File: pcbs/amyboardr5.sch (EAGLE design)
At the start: 152 parts, among them Q2 S8050, Q5 S8050, U1 PCM9211PT, U15 H11L1SR2M, U16 SPX3819, U2 ESP32­S2­SOLO, U3 SPX3819, U4 TL074CD, U6 HX3608, Y1 22.5792MHZ

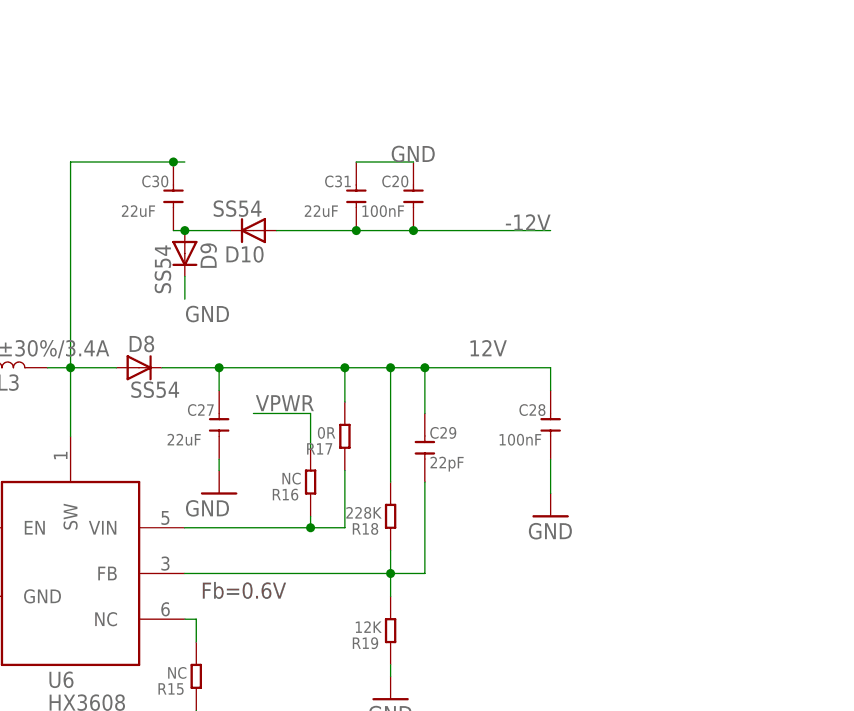
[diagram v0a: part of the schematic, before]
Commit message: Added ferrite beads in Pi circuits to + and -12v lines.
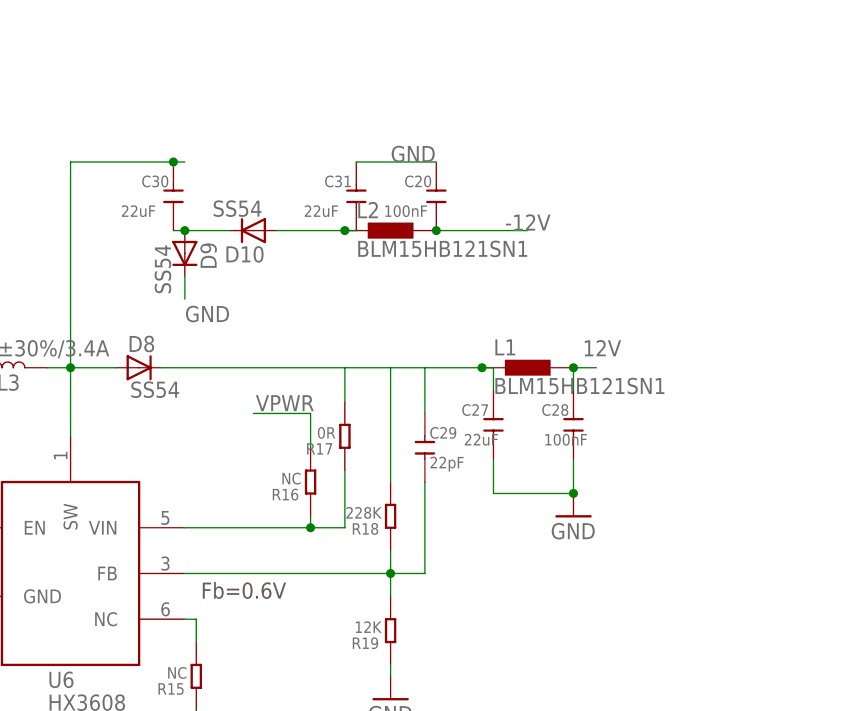
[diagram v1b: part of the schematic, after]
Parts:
- added L1, L2: BLM15HB121SN1, inductors:BLM15HB121SN1
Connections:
- new net N$16: C31.2, D10.A, L2.1
- new net N$24: C27.1, D8.C, L1.1
- new net N$25: C29.1
- new net N$30: R18.2
- net -12V: now also L2.2; no longer C31.2, D10.A
- net 12V: now also L1.2; no longer C27.1, C29.1, D8.C, R18.2
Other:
- moved on the sheet: C20, C27, C28
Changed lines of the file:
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@@
 <part name="GND5" library="supply1" deviceset="GND" device=""/>
 <part name="R14" library="A9G" deviceset="DISCRETE_R*" device="-0603" value="100K"/>
-<part name="GND6" library="supply1" deviceset="GND" device=""/>
 <part name="R15" library="A9G" deviceset="DISCRETE_R*" device="-0603" value="NC"/>
 <part name="R16" library="A9G" deviceset="DISCRETE_R*" device="-0603" value="NC"/>
@@
 <part name="R6" library="adafruit" deviceset="R-US_" device="R0805" value="10K"/>
 <part name="R8" library="adafruit" deviceset="R-US_" device="R0805" value="15K"/>
+<part name="L1" library="inductors" library_urn="urn:adsk.eagle:library:243" deviceset="BLM15H" device="" package3d_urn="urn:adsk.eagle:package:15132/1" technology="B121SN1"/>
+<part name="L2" library="inductors" library_urn="urn:adsk.eagle:library:243" deviceset="BLM15H" device="" package3d_urn="urn:adsk.eagle:package:15132/1" technology="B121SN1"/>
 </parts>
 <sheets>
@@
 <attribute name="VALUE" x="242.824" y="-8.4074" size="1.778" layer="96"/>
 </instance>
-<instance part="C27" gate="C" x="252.73" y="-11.43" smashed="yes" rot="R270">
-<attribute name="NAME" x="249.174" y="-10.414" size="1.27" layer="95" ratio="10"/>
-<attribute name="VALUE" x="246.888" y="-13.716" size="1.27" layer="96" ratio="10"/>
-</instance>
-<instance part="C28" gate="C" x="289.56" y="-11.43" smashed="yes" rot="R270">
-<attribute name="NAME" x="286.004" y="-10.414" size="1.27" layer="95" ratio="10"/>
-<attribute name="VALUE" x="283.718" y="-13.716" size="1.27" layer="96" ratio="10"/>
+<instance part="C27" gate="C" x="283.21" y="-11.43" smashed="yes" rot="R270">
+<attribute name="NAME" x="279.654" y="-10.414" size="1.27" layer="95" ratio="10"/>
+<attribute name="VALUE" x="279.908" y="-13.716" size="1.27" layer="96" ratio="10"/>
+</instance>
+<instance part="C28" gate="C" x="292.1" y="-11.43" smashed="yes" rot="R270">
+<attribute name="NAME" x="288.544" y="-10.414" size="1.27" layer="95" ratio="10"/>
+<attribute name="VALUE" x="288.798" y="-13.716" size="1.27" layer="96" ratio="10"/>
 </instance>
 <instance part="C29" gate="C" x="275.59" y="-13.97" smashed="yes" rot="R270">
@@
 <attribute name="VALUE" x="269.24" y="-44.45" size="1.778" layer="96"/>
 </instance>
-<instance part="GND5" gate="1" x="289.56" y="-21.59" smashed="yes">
-<attribute name="VALUE" x="287.02" y="-24.13" size="1.778" layer="96"/>
+<instance part="GND5" gate="1" x="292.1" y="-21.59" smashed="yes">
+<attribute name="VALUE" x="289.56" y="-24.13" size="1.778" layer="96"/>
 </instance>
 <instance part="R14" gate="R" x="220.98" y="-13.97" smashed="yes" rot="R90">
@@
 <attribute name="VALUE" x="219.964" y="-12.954" size="1.27" layer="96" ratio="10" rot="R180"/>
 </instance>
-<instance part="GND6" gate="1" x="252.73" y="-19.05" smashed="yes">
-<attribute name="VALUE" x="248.92" y="-21.59" size="1.778" layer="96"/>
-</instance>
 <instance part="R15" gate="R" x="250.19" y="-39.37" smashed="yes" rot="R90">
 <attribute name="NAME" x="248.92" y="-40.132" size="1.27" layer="95" ratio="10" rot="R180"/>
@@
 <attribute name="VALUE" x="262.128" y="11.684" size="1.27" layer="96" ratio="10"/>
 </instance>
-<instance part="C20" gate="C" x="274.32" y="13.97" smashed="yes" rot="R270">
-<attribute name="NAME" x="270.764" y="14.986" size="1.27" layer="95" ratio="10"/>
-<attribute name="VALUE" x="268.478" y="11.684" size="1.27" layer="96" ratio="10"/>
+<instance part="C20" gate="C" x="276.86" y="13.97" smashed="yes" rot="R270">
+<attribute name="NAME" x="273.304" y="14.986" size="1.27" layer="95" ratio="10"/>
+<attribute name="VALUE" x="271.018" y="11.684" size="1.27" layer="96" ratio="10"/>
 </instance>
 <instance part="C21" gate="C" x="-137.16" y="-46.99" smashed="yes" rot="R270">
@@
 <attribute name="VALUE" x="-99.06" y="-28.702" size="1.016" layer="96" font="vector" ratio="15" rot="R270"/>
 </instance>
+<instance part="L1" gate="G$1" x="287.02" y="-5.08" smashed="yes">
+<attribute name="NAME" x="283.21" y="-3.7084" size="1.778" layer="95"/>
+<attribute name="VALUE" x="283.21" y="-8.001" size="1.778" layer="96"/>
+</instance>
+<instance part="L2" gate="G$1" x="271.78" y="10.16" smashed="yes">
+<attribute name="NAME" x="267.97" y="11.5316" size="1.778" layer="95"/>
+<attribute name="VALUE" x="267.97" y="7.239" size="1.778" layer="96"/>
+</instance>
 </instances>
 <busses>
@@
 <segment>
 <pinref part="C28" gate="C" pin="2"/>
-<wire x1="289.56" y1="-19.05" x2="289.56" y2="-15.24" width="0.1524" layer="91"/>
+<wire x1="292.1" y1="-19.05" x2="292.1" y2="-15.24" width="0.1524" layer="91"/>
 <pinref part="GND5" gate="1" pin="GND"/>
-</segment>
-<segment>
-<pinref part="GND6" gate="1" pin="GND"/>
 <pinref part="C27" gate="C" pin="2"/>
-<wire x1="252.73" y1="-16.51" x2="252.73" y2="-15.24" width="0.1524" layer="91"/>
+<wire x1="283.21" y1="-15.24" x2="283.21" y2="-19.05" width="0.1524" layer="91"/>
+<wire x1="283.21" y1="-19.05" x2="292.1" y2="-19.05" width="0.1524" layer="91"/>
+<junction x="292.1" y="-19.05"/>
 </segment>
 <segment>
@@
 <segment>
 <pinref part="C31" gate="C" pin="1"/>
-<wire x1="267.97" y1="17.78" x2="274.32" y2="17.78" width="0.1524" layer="91"/>
+<wire x1="267.97" y1="17.78" x2="276.86" y2="17.78" width="0.1524" layer="91"/>
 <label x="271.78" y="17.78" size="1.778" layer="95"/>
 <pinref part="C20" gate="C" pin="1"/>
@@
 <net name="-12V" class="0">
 <segment>
-<pinref part="D10" gate="G$1" pin="A"/>
-<pinref part="C31" gate="C" pin="2"/>
-<wire x1="259.08" y1="10.16" x2="267.97" y2="10.16" width="0.1524" layer="91"/>
-<wire x1="267.97" y1="10.16" x2="274.32" y2="10.16" width="0.1524" layer="91"/>
-<junction x="267.97" y="10.16"/>
 <label x="284.48" y="10.16" size="1.778" layer="95"/>
 <pinref part="C20" gate="C" pin="2"/>
-<wire x1="274.32" y1="10.16" x2="289.56" y2="10.16" width="0.1524" layer="91"/>
-<junction x="274.32" y="10.16"/>
+<wire x1="276.86" y1="10.16" x2="287.02" y2="10.16" width="0.1524" layer="91"/>
+<pinref part="L2" gate="G$1" pin="2"/>
+<junction x="276.86" y="10.16"/>
 </segment>
 <segment>
@@
 <net name="12V" class="0">
 <segment>
-<pinref part="C28" gate="C" pin="1"/>
-<wire x1="289.56" y1="-5.08" x2="289.56" y2="-7.62" width="0.1524" layer="91"/>
-<pinref part="C27" gate="C" pin="1"/>
-<wire x1="252.73" y1="-7.62" x2="252.73" y2="-5.08" width="0.1524" layer="91"/>
-<pinref part="D8" gate="G$1" pin="C"/>
-<wire x1="252.73" y1="-5.08" x2="246.38" y2="-5.08" width="0.1524" layer="91"/>
-<wire x1="252.73" y1="-5.08" x2="266.7" y2="-5.08" width="0.1524" layer="91"/>
-<junction x="252.73" y="-5.08"/>
-<wire x1="266.7" y1="-5.08" x2="271.78" y2="-5.08" width="0.1524" layer="91"/>
-<wire x1="271.78" y1="-5.08" x2="271.78" y2="-17.78" width="0.1524" layer="91"/>
-<wire x1="271.78" y1="-5.08" x2="275.59" y2="-5.08" width="0.1524" layer="91"/>
-<junction x="271.78" y="-5.08"/>
-<wire x1="275.59" y1="-5.08" x2="289.56" y2="-5.08" width="0.1524" layer="91"/>
-<pinref part="C29" gate="C" pin="1"/>
-<wire x1="275.59" y1="-10.16" x2="275.59" y2="-5.08" width="0.1524" layer="91"/>
-<junction x="275.59" y="-5.08"/>
-<label x="280.416" y="-3.81" size="1.778" layer="95"/>
 <wire x1="266.7" y1="-8.89" x2="266.7" y2="-5.08" width="0.1524" layer="91"/>
-<junction x="266.7" y="-5.08"/>
 <pinref part="R17" gate="R" pin="2"/>
-<pinref part="R18" gate="R" pin="2"/>
 </segment>
 <segment>
@@
 <junction x="167.64" y="-11.43"/>
 </segment>
+<segment>
+<pinref part="C28" gate="C" pin="1"/>
+<wire x1="292.1" y1="-5.08" x2="294.64" y2="-5.08" width="0.1524" layer="91"/>
+<wire x1="292.1" y1="-5.08" x2="292.1" y2="-7.62" width="0.1524" layer="91"/>
+<label x="293.116" y="-3.81" size="1.778" layer="95"/>
+<pinref part="L1" gate="G$1" pin="2"/>
+<junction x="292.1" y="-5.08"/>
+</segment>
 </net>
 <net name="N$29" class="0">
@@
 </segment>
 </net>
+<net name="N$16" class="0">
+<segment>
+<pinref part="C31" gate="C" pin="2"/>
+<pinref part="D10" gate="G$1" pin="A"/>
+<wire x1="259.08" y1="10.16" x2="266.7" y2="10.16" width="0.1524" layer="91"/>
+<pinref part="L2" gate="G$1" pin="1"/>
+<wire x1="266.7" y1="10.16" x2="267.97" y2="10.16" width="0.1524" layer="91"/>
+<junction x="266.7" y="10.16"/>
+</segment>
+</net>
+<net name="N$24" class="0">
+<segment>
+<pinref part="L1" gate="G$1" pin="1"/>
+<wire x1="281.94" y1="-5.08" x2="283.21" y2="-5.08" width="0.1524" layer="91"/>
+<pinref part="C27" gate="C" pin="1"/>
+<wire x1="283.21" y1="-7.62" x2="283.21" y2="-5.08" width="0.1524" layer="91"/>
+<pinref part="D8" gate="G$1" pin="C"/>
+<wire x1="246.38" y1="-5.08" x2="281.94" y2="-5.08" width="0.1524" layer="91"/>
+<junction x="281.94" y="-5.08"/>
+</segment>
+</net>
+<net name="N$25" class="0">
+<segment>
+<pinref part="C29" gate="C" pin="1"/>
+<wire x1="275.59" y1="-10.16" x2="275.59" y2="-5.08" width="0.1524" layer="91"/>
+</segment>
+</net>
+<net name="N$30" class="0">
+<segment>
+<wire x1="271.78" y1="-5.08" x2="271.78" y2="-17.78" width="0.1524" layer="91"/>
+<pinref part="R18" gate="R" pin="2"/>
+</segment>
+</net>

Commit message: Moved GP8413 and 5V LDO to +12V_UNFILTERED.
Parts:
- removed C21: 20pF, Discrete-new:CAP-0603
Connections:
- removed net N$24: C27.1, D8.C, L1.1
- new net 12V_UNFILTERED: C26.1, C27.1, C32.1, D8.C, L1.1, U$7.VCC, U3.EN, U3.VIN
- net +12V: no longer C21.1, C26.1, U$7.VCC
- net -12V: no longer C21.2
- net 12V: no longer C32.1, U3.EN, U3.VIN
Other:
- note added: "Place C20 and C28 close to U4 (TL074)"
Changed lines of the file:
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@@
 <part name="C31" library="Discrete-new" deviceset="CAP" device="-0603" value="22uF"/>
 <part name="C20" library="Discrete-new" deviceset="CAP" device="-0603" value="100nF"/>
-<part name="C21" library="Discrete-new" deviceset="CAP" device="-0603" value="20pF"/>
 <part name="R20" library="adafruit" deviceset="R-US_" device="R0805" value="10K"/>
 <part name="R21" library="adafruit" deviceset="R-US_" device="R0805" value="15K"/>
@@
 <rectangle x1="132.08" y1="-38.1" x2="152.4" y2="25.4" layer="200"/>
 <text x="157.226" y="184.658" size="5.08" layer="97">PCM5101 DAC</text>
+<text x="299.72" y="5.08" size="1.778" layer="91">Place C20 and C28
+close to U4 (TL074)</text>
 </plain>
 <instances>
@@
 <attribute name="VALUE" x="271.018" y="11.684" size="1.27" layer="96" ratio="10"/>
 </instance>
-<instance part="C21" gate="C" x="-137.16" y="-46.99" smashed="yes" rot="R270">
-<attribute name="NAME" x="-140.716" y="-45.974" size="1.27" layer="95" ratio="10"/>
-<attribute name="VALUE" x="-143.002" y="-49.276" size="1.27" layer="96" ratio="10"/>
-</instance>
 <instance part="R20" gate="G$1" x="-78.74" y="-53.34" smashed="yes" rot="R270">
 <attribute name="NAME" x="-77.724" y="-51.054" size="1.27" layer="95" font="vector" rot="R270"/>
@@
 <wire x1="-137.16" y1="-48.26" x2="-137.16" y2="-50.8" width="0.1524" layer="91"/>
 <label x="-137.16" y="-50.8" size="1.778" layer="95"/>
-<pinref part="C21" gate="C" pin="2"/>
 </segment>
 </net>
@@
 <pinref part="U4" gate="A" pin="VCC+"/>
 <wire x1="-142.24" y1="-45.72" x2="-137.16" y2="-45.72" width="0.1524" layer="91"/>
-<wire x1="-137.16" y1="-45.72" x2="-137.16" y2="-43.18" width="0.1524" layer="91"/>
 <label x="-137.16" y="-40.64" size="1.778" layer="95"/>
-<pinref part="C21" gate="C" pin="1"/>
-<wire x1="-137.16" y1="-43.18" x2="-137.16" y2="-40.64" width="0.1524" layer="91"/>
-<junction x="-137.16" y="-43.18"/>
-</segment>
-<segment>
-<pinref part="U$7" gate="G$1" pin="VCC"/>
-<wire x1="-181.61" y1="-15.24" x2="-187.96" y2="-15.24" width="0.1524" layer="91"/>
-<wire x1="-187.96" y1="-15.24" x2="-198.12" y2="-15.24" width="0.1524" layer="91"/>
-<wire x1="-198.12" y1="-15.24" x2="-198.12" y2="-10.16" width="0.1524" layer="91"/>
-<label x="-198.12" y="-10.16" size="1.778" layer="95"/>
-<pinref part="C26" gate="G$1" pin="1"/>
-<junction x="-187.96" y="-15.24"/>
+<wire x1="-137.16" y1="-45.72" x2="-137.16" y2="-40.64" width="0.1524" layer="91"/>
 </segment>
 </net>
@@
 </segment>
 <segment>
-<wire x1="165.1" y1="-12.7" x2="165.1" y2="-11.43" width="0.1524" layer="91"/>
-<pinref part="C32" gate="C" pin="1"/>
-<label x="161.544" y="-10.922" size="1.778" layer="95"/>
-<pinref part="U3" gate="G$1" pin="VIN"/>
-<wire x1="168.91" y1="-11.43" x2="167.64" y2="-11.43" width="0.1524" layer="91"/>
-<pinref part="U3" gate="G$1" pin="EN"/>
-<wire x1="167.64" y1="-11.43" x2="165.1" y2="-11.43" width="0.1524" layer="91"/>
-<wire x1="168.91" y1="-13.97" x2="167.64" y2="-13.97" width="0.1524" layer="91"/>
-<wire x1="167.64" y1="-13.97" x2="167.64" y2="-11.43" width="0.1524" layer="91"/>
-<junction x="167.64" y="-11.43"/>
-</segment>
-<segment>
 <pinref part="C28" gate="C" pin="1"/>
 <wire x1="292.1" y1="-5.08" x2="294.64" y2="-5.08" width="0.1524" layer="91"/>
@@
 </segment>
 </net>
-<net name="N$24" class="0">
+<net name="12V_UNFILTERED" class="0">
 <segment>
 <pinref part="L1" gate="G$1" pin="1"/>
@@
 <wire x1="246.38" y1="-5.08" x2="281.94" y2="-5.08" width="0.1524" layer="91"/>
 <junction x="281.94" y="-5.08"/>
+<label x="256.54" y="-5.08" size="1.778" layer="95"/>
+</segment>
+<segment>
+<pinref part="U3" gate="G$1" pin="VIN"/>
+<pinref part="C32" gate="C" pin="1"/>
+<wire x1="168.91" y1="-11.43" x2="165.1" y2="-11.43" width="0.1524" layer="91"/>
+<wire x1="165.1" y1="-11.43" x2="165.1" y2="-12.7" width="0.1524" layer="91"/>
+<pinref part="U3" gate="G$1" pin="EN"/>
+<wire x1="168.91" y1="-11.43" x2="168.91" y2="-13.97" width="0.1524" layer="91"/>
+<junction x="168.91" y="-11.43"/>
+<wire x1="165.1" y1="-10.16" x2="165.1" y2="-5.08" width="0.1524" layer="91"/>
+<wire x1="165.1" y1="-10.16" x2="165.1" y2="-12.7" width="0.1524" layer="91"/>
+<junction x="165.1" y="-12.7"/>
+<label x="165.1" y="-5.08" size="1.778" layer="95"/>
+</segment>
+<segment>
+<pinref part="U$7" gate="G$1" pin="VCC"/>
+<pinref part="C26" gate="G$1" pin="1"/>
+<wire x1="-181.61" y1="-15.24" x2="-187.96" y2="-15.24" width="0.1524" layer="91"/>
+<wire x1="-187.96" y1="-15.24" x2="-193.04" y2="-15.24" width="0.1524" layer="91"/>
+<junction x="-187.96" y="-15.24"/>
+<wire x1="-193.04" y1="-15.24" x2="-193.04" y2="-10.16" width="0.1524" layer="91"/>
+<label x="-213.36" y="-12.7" size="1.778" layer="95"/>
 </segment>
 </net>

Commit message: copying usb fb
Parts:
- removed L1, L2: BLM15HB121SN1, inductors:BLM15HB121SN1
- added FB1, FB2: 100Mhz@120R, rcl:R-EU_R0805
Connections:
- net -12V: now also FB1.2; no longer L2.2
- net 12V: now also FB2.2; no longer L1.2
- net 12V_UNFILTERED: now also FB2.1; no longer L1.1
- net N$16: now also FB1.1; no longer L2.1
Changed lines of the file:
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@@
 <part name="R6" library="adafruit" deviceset="R-US_" device="R0805" value="10K"/>
 <part name="R8" library="adafruit" deviceset="R-US_" device="R0805" value="15K"/>
-<part name="L1" library="inductors" library_urn="urn:adsk.eagle:library:243" deviceset="BLM15H" device="" package3d_urn="urn:adsk.eagle:package:15132/1" technology="B121SN1"/>
-<part name="L2" library="inductors" library_urn="urn:adsk.eagle:library:243" deviceset="BLM15H" device="" package3d_urn="urn:adsk.eagle:package:15132/1" technology="B121SN1"/>
+<part name="FB1" library="rcl" deviceset="R-EU_" device="R0805" value="100Mhz@120R"/>
+<part name="FB2" library="rcl" deviceset="R-EU_" device="R0805" value="100Mhz@120R"/>
 </parts>
 <sheets>
@@
 <attribute name="VALUE" x="-99.06" y="-28.702" size="1.016" layer="96" font="vector" ratio="15" rot="R270"/>
 </instance>
-<instance part="L1" gate="G$1" x="287.02" y="-5.08" smashed="yes">
-<attribute name="NAME" x="283.21" y="-3.7084" size="1.778" layer="95"/>
-<attribute name="VALUE" x="283.21" y="-8.001" size="1.778" layer="96"/>
-</instance>
-<instance part="L2" gate="G$1" x="271.78" y="10.16" smashed="yes">
-<attribute name="NAME" x="267.97" y="11.5316" size="1.778" layer="95"/>
-<attribute name="VALUE" x="267.97" y="7.239" size="1.778" layer="96"/>
+<instance part="FB1" gate="G$1" x="273.05" y="10.16" smashed="yes">
+<attribute name="NAME" x="270.764" y="11.9126" size="1.778" layer="95"/>
+<attribute name="VALUE" x="264.16" y="14.732" size="1.778" layer="96"/>
+</instance>
+<instance part="FB2" gate="G$1" x="288.29" y="-5.08" smashed="yes">
+<attribute name="NAME" x="286.004" y="-3.3274" size="1.778" layer="95"/>
+<attribute name="VALUE" x="279.4" y="-0.508" size="1.778" layer="96"/>
 </instance>
 </instances>
@@
 <label x="284.48" y="10.16" size="1.778" layer="95"/>
 <pinref part="C20" gate="C" pin="2"/>
-<wire x1="276.86" y1="10.16" x2="287.02" y2="10.16" width="0.1524" layer="91"/>
-<pinref part="L2" gate="G$1" pin="2"/>
-<junction x="276.86" y="10.16"/>
+<wire x1="276.86" y1="10.16" x2="278.13" y2="10.16" width="0.1524" layer="91"/>
+<pinref part="FB1" gate="G$1" pin="2"/>
+<wire x1="278.13" y1="10.16" x2="287.02" y2="10.16" width="0.1524" layer="91"/>
+<junction x="278.13" y="10.16"/>
 </segment>
 <segment>
@@
 <segment>
 <pinref part="C28" gate="C" pin="1"/>
-<wire x1="292.1" y1="-5.08" x2="294.64" y2="-5.08" width="0.1524" layer="91"/>
+<wire x1="292.1" y1="-5.08" x2="293.37" y2="-5.08" width="0.1524" layer="91"/>
+<wire x1="293.37" y1="-5.08" x2="294.64" y2="-5.08" width="0.1524" layer="91"/>
 <wire x1="292.1" y1="-5.08" x2="292.1" y2="-7.62" width="0.1524" layer="91"/>
 <label x="293.116" y="-3.81" size="1.778" layer="95"/>
-<pinref part="L1" gate="G$1" pin="2"/>
-<junction x="292.1" y="-5.08"/>
+<pinref part="FB2" gate="G$1" pin="2"/>
+<junction x="293.37" y="-5.08"/>
 </segment>
 </net>
@@
 <pinref part="C31" gate="C" pin="2"/>
 <pinref part="D10" gate="G$1" pin="A"/>
-<wire x1="259.08" y1="10.16" x2="266.7" y2="10.16" width="0.1524" layer="91"/>
-<pinref part="L2" gate="G$1" pin="1"/>
-<wire x1="266.7" y1="10.16" x2="267.97" y2="10.16" width="0.1524" layer="91"/>
-<junction x="266.7" y="10.16"/>
+<wire x1="259.08" y1="10.16" x2="267.97" y2="10.16" width="0.1524" layer="91"/>
+<pinref part="FB1" gate="G$1" pin="1"/>
+<junction x="267.97" y="10.16"/>
 </segment>
 </net>
 <net name="12V_UNFILTERED" class="0">
 <segment>
-<pinref part="L1" gate="G$1" pin="1"/>
-<wire x1="281.94" y1="-5.08" x2="283.21" y2="-5.08" width="0.1524" layer="91"/>
 <pinref part="C27" gate="C" pin="1"/>
 <wire x1="283.21" y1="-7.62" x2="283.21" y2="-5.08" width="0.1524" layer="91"/>
 <pinref part="D8" gate="G$1" pin="C"/>
-<wire x1="246.38" y1="-5.08" x2="281.94" y2="-5.08" width="0.1524" layer="91"/>
-<junction x="281.94" y="-5.08"/>
+<wire x1="246.38" y1="-5.08" x2="283.21" y2="-5.08" width="0.1524" layer="91"/>
 <label x="256.54" y="-5.08" size="1.778" layer="95"/>
+<pinref part="FB2" gate="G$1" pin="1"/>
+<junction x="283.21" y="-5.08"/>
 </segment>
 <segment>
